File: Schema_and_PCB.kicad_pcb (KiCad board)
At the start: 4 copper layers, 293.6 x 143.3 mm, 217 parts, among them J1 USB4085-GF-A_REVA, J11 Pulse_JXD6-0001NL, J12 Ground, J13 640456-2, J14 640456-3, J15 640456-3, J16 0022232041, J17 0022232041, J2 OSTTC020162, J3 302-S101, J4 DM3AT-SF-PEJM5, J5 OSTTC020162, J7 OSTTC030162, J9 0022232031, Q1 BC817-25LT1G, Q2 BC817-25LT1G, Q3 BC817-25LT1G, Q4 BC817-25LT1G, SW1 SW_PUSHBUTTON, SW2 SW_PUSHBUTTON, SW3 SW_PUSHBUTTON, SW4 SW_PUSHBUTTON, SW5 SW_PUSHBUTTON, SW6 SW_PUSHBUTTON, U1 CC56-12SURKWA, U10 TLV75529PDBV, U11 STM32H743ZIT6, U12 LD1117S33CTR, U13 LD1117S33CTR, U14 SN74AVCA406DGGR, U15 W25Q256JVFIQ, U17 ISO1211DR, U2 CC56-12SURKWA, U24 ISO1211DR, U26 ISO1211DR, U3 MAX7219EWG+T, U30 LAN8742A-CZ-TR, U4 BC56-12SURKWA, U5 SC56-11SRWA, U6 MAX7219EWG+T, U7 CC56-12SURKWA, U8 ADUM4160, U9 ST1L05APU33R, Y1 NX5032GA-8MHz, Y2 NX3215SA-32.768K-STD-MUA-14, Y3 NX2016SA-25MHz

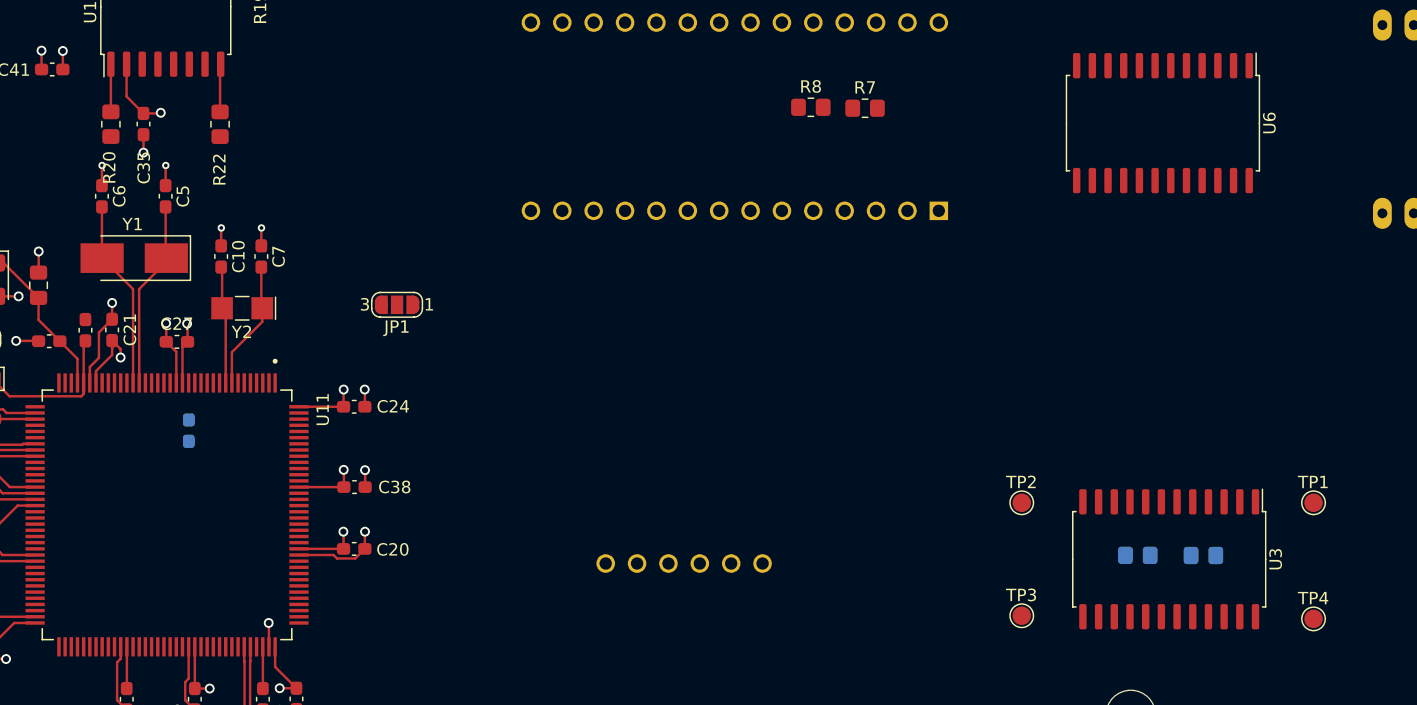
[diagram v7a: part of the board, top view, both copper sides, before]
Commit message: Change ADC3 input chanel and pin
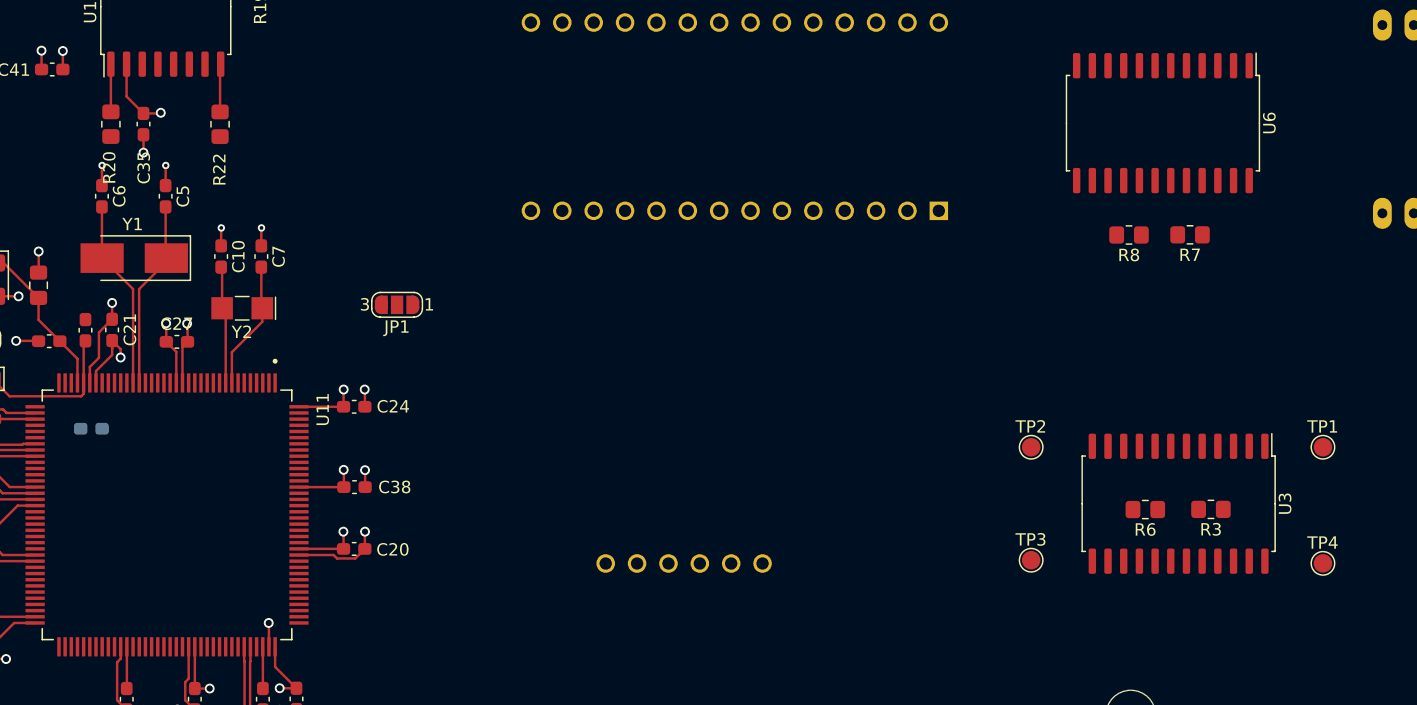
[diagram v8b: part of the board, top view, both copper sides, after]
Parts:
- R3, R6: moved to F.Cu
- moved R7 28.2 mm to (221.9, 122.6), turned to 180 degrees
- moved R8 27.8 mm to (217.0, 122.6), turned to 180 degrees
- moved C50 7.89 mm to (133.0, 138.3), turned to 180 degrees
- moved TP1 4.56 mm to (232.7, 139.8)
- moved TP2 4.56 mm to (209.0, 139.8)
- moved TP3 4.56 mm to (209.0, 148.9)
- moved U3 4.56 mm to (221.0, 144.3)
- moved TP4 4.56 mm to (232.7, 149.2)
- moved R3 3.78 mm to (223.6, 144.8)
- moved R6 3.76 mm to (218.3, 144.8)
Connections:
- U11 pad 15: /Digital_IO_analog_Inputs/ADC3_P -> Net-(U11-Pad15)
- U11 pad 29: Net-(U11-Pad29) -> /Digital_IO_analog_Inputs/ADC3_P
